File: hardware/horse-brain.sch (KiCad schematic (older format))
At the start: 12 parts

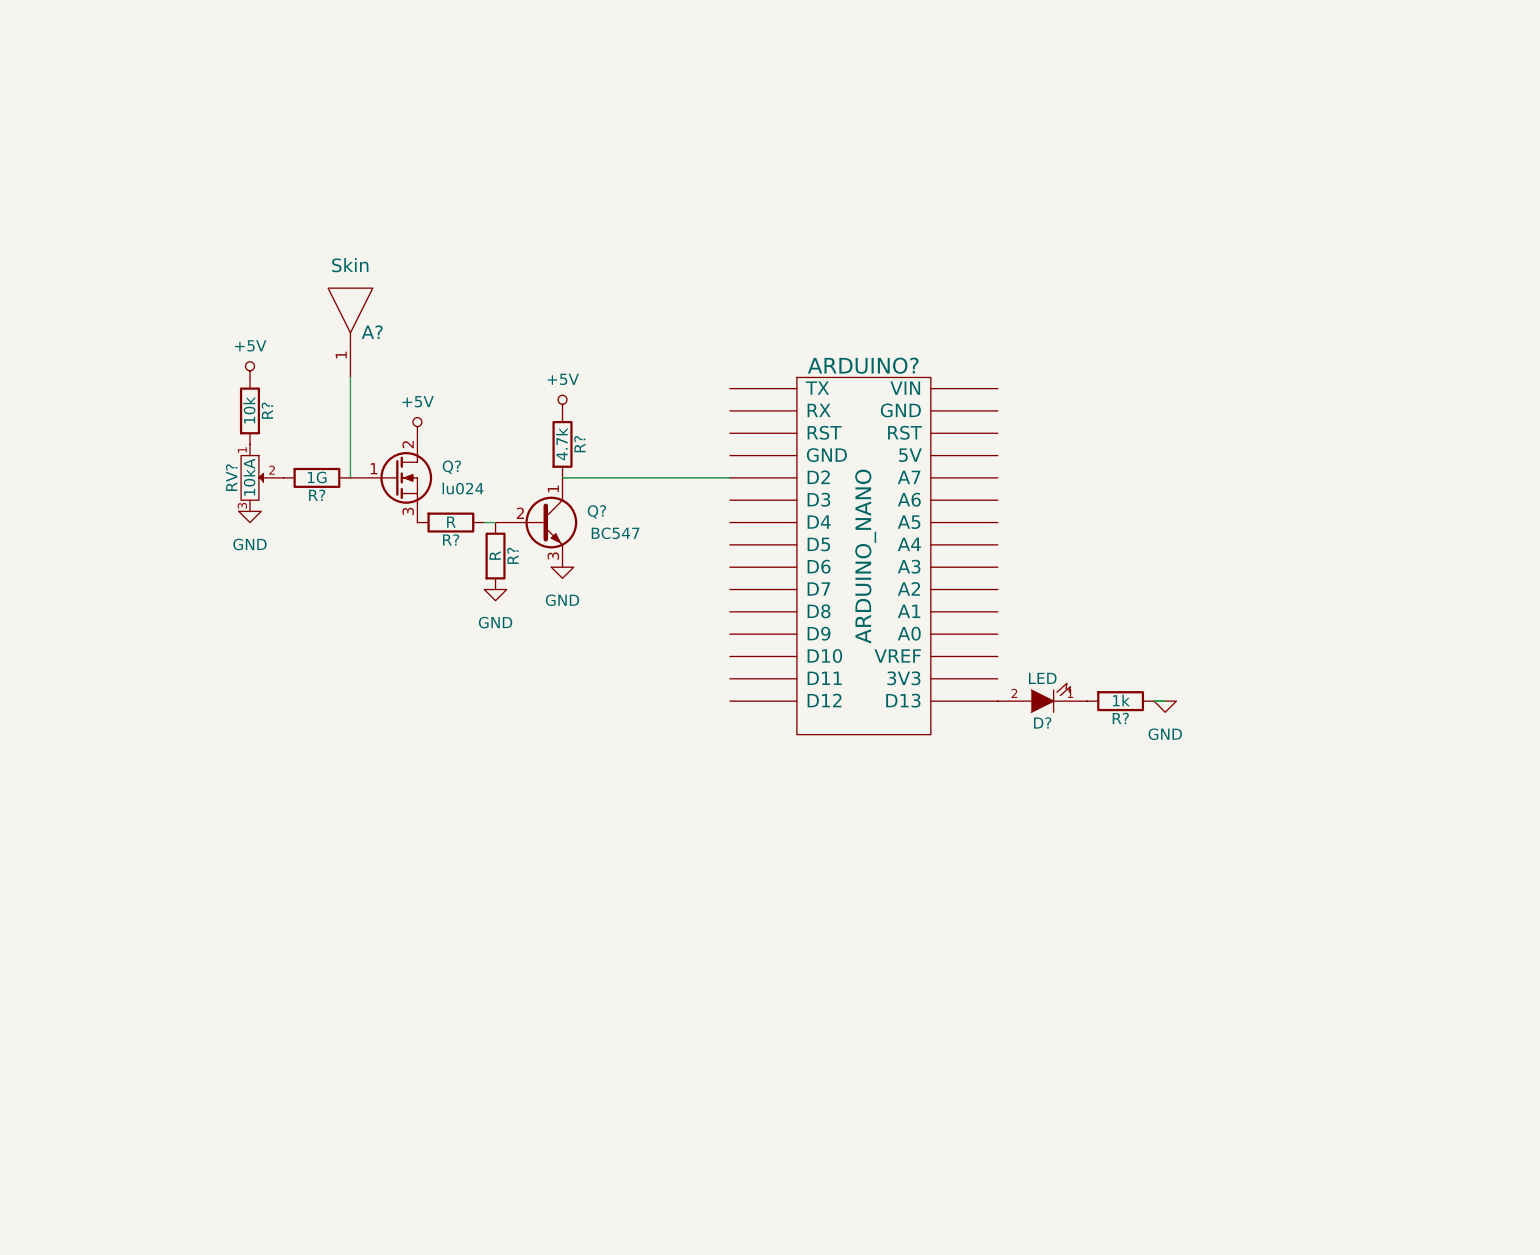
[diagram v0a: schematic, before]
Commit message: Add inverter interface to schematic
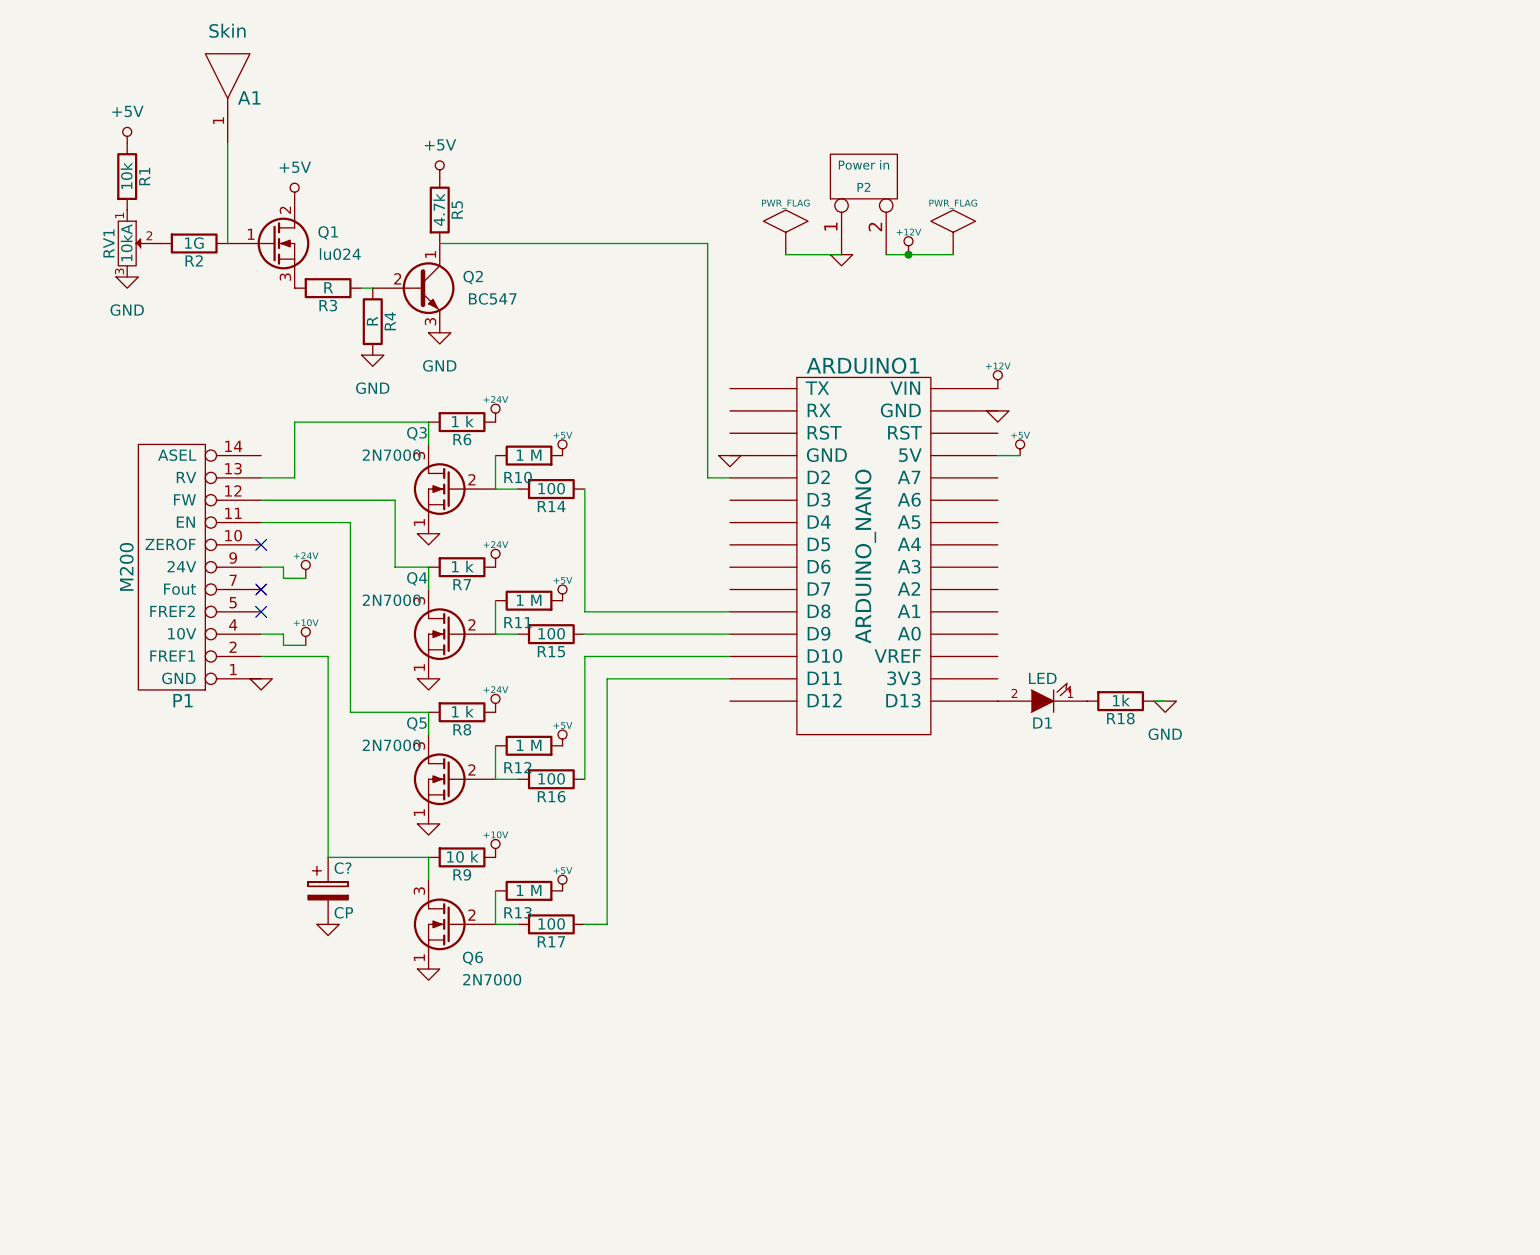
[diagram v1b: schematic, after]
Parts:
- added C?: CP, symbol CP
- added P1: M200, symbol M200
- added P2: Power in, symbol CONN_2
- added Q3, Q4, Q5, Q6: 2N7000, symbol Q_NMOS_SGD
- added R10, R11, R12, R13: 1 M, symbol R
- added R14, R15, R16, R17: 100, symbol R
- added R6, R7, R8: 1 k, symbol R
- added R9: 10 k, symbol R
- gave numbers to parts that had none: 12
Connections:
- net +5V: now also ARDUINO1.27 (5V), R10.2, R11.2, R12.2, R13.2
- net GND: now also ARDUINO1.29 (GND), ARDUINO1.4 (GND), C?.2, P1.1 (GND), P2.1 (P1), Q3.1 (S), Q4.1 (S), Q5.1 (S), Q6.1 (S)
- net at ARDUINO1.11 (D8): now also R14.1
- net at ARDUINO1.12 (D9): now also R15.1
- net at ARDUINO1.13 (D10): now also R16.1
- net at ARDUINO1.14 (D11): now also R17.1
- net +12V: now reaches ARDUINO1.30 (VIN)
- net +12V: now also P2.2 (PM)
- new net: P1.11 (EN), Q5.3 (D), R8.2
- new net: P1.12 (FW), Q4.3 (D), R7.2
- new net: P1.13 (RV), Q3.3 (D), R6.2
- new net: C?.1, P1.2 (FREF1), Q6.3 (D), R9.2
- new net: Q3.2 (G), R10.1, R14.2
- new net: Q4.2 (G), R11.1, R15.2
- new net: Q5.2 (G), R12.1, R16.2
- new net: Q6.2 (G), R13.1, R17.2
- new net +10V: P1.4 (10V), R9.1
- new net +24V: P1.9 (24V), R6.1, R7.1, R8.1
- no-connect marks 0 -> 3
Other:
- moved on the sheet: A1, Q1, Q2, R1, R2, R3, R4, R5, RV1

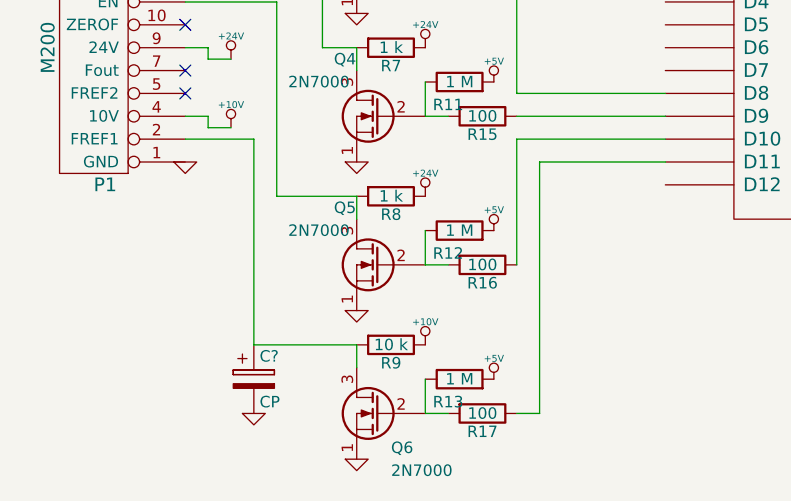
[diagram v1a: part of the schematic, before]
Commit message: First version of motor control code
Ensures that the interface to inverter works, but does not do anything
sensible yet. Also, there is a simplification regarding analog input to
inverter.
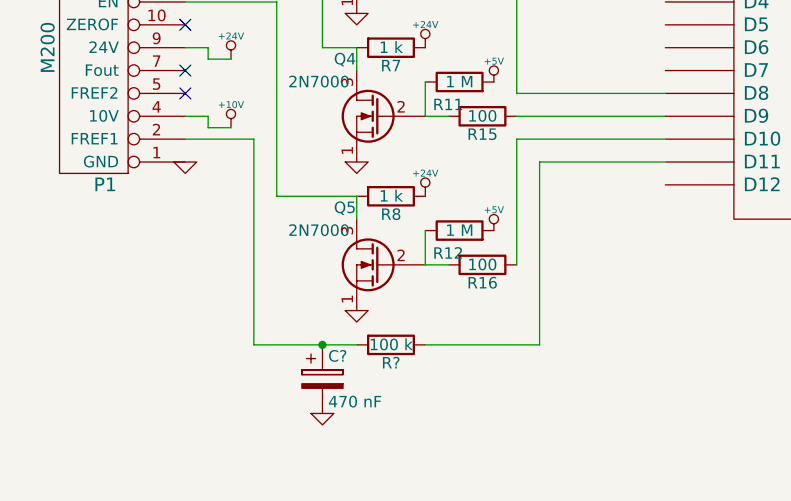
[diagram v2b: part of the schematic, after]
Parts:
- removed C?: CP, symbol CP
- removed Q6: 2N7000, symbol Q_NMOS_SGD
- removed R13: 1 M, symbol R
- removed R17: 100, symbol R
- removed R9: 10 k, symbol R
- added C?: 470 nF, symbol CP
- added R?: 100 k, symbol R
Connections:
- net GND: now also C?.2
- net at ARDUINO1.14 (D11): now also R?.1
- net at P1.2 (FREF1): now also C?.1, R?.2
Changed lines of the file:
@@
-	1    0    0    -1
-$EndComp
-$Comp
-L Q_NMOS_SGD Q6
-U 1 1 583F98D2
-P 4850 5500
-F 0 "Q6" H 4800 5350 50  0000 R CNN
-F 1 "2N7000" H 4800 5250 50  0000 R CNN
-F 2 "" H 5050 5600 50  0000 C CNN
-F 3 "" H 4850 5500 50  0000 C CNN
-	1    4850 5500
-	-1   0    0    -1
-$EndComp
-$Comp
-L R R13
-U 1 1 583F98D8
-P 5200 5350
-F 0 "R13" V 5100 5400 50  0000 C CNN
-F 1 "1 M" V 5200 5350 50  0000 C CNN
-F 2 "" V 5130 5350 50  0000 C CNN
-F 3 "" H 5200 5350 50  0000 C CNN
-	1    5200 5350
-	0    -1   -1   0
-$EndComp
-$Comp
-L R R17
-U 1 1 583F98DE
-P 5300 5500
-F 0 "R17" V 5380 5500 50  0000 C CNN
-F 1 "100" V 5300 5500 50  0000 C CNN
-F 2 "" V 5230 5500 50  0000 C CNN
-F 3 "" H 5300 5500 50  0000 C CNN
-	1    5300 5500
-	0    1    1    0
-$EndComp
-Wire Wire Line
-	5050 5500 5150 5500
-$Comp
-L +5V #PWR024
-U 1 1 583F98E5
-P 5350 5350
-F 0 "#PWR024" H 5350 5440 20  0001 C CNN
-F 1 "+5V" H 5350 5440 30  0000 C CNN
-F 2 "" H 5350 5350 60  0001 C CNN
-F 3 "" H 5350 5350 60  0001 C CNN
-	1    5350 5350
-	1    0    0    -1
-$EndComp
-Wire Wire Line
-	5050 5500 5050 5350
-$Comp
-L R R9
-U 1 1 583F98EC
-P 4900 5200
-F 0 "R9" V 4980 5200 50  0000 C CNN
-F 1 "10 k" V 4900 5200 50  0000 C CNN
-F 2 "" V 4830 5200 50  0000 C CNN
-F 3 "" H 4900 5200 50  0000 C CNN
-	1    4900 5200
-	0    1    1    0
-$EndComp
-Wire Wire Line
-	4750 5200 4750 5300
-$Comp
-L GND #PWR025
-U 1 1 583F98F9
-P 4750 5700
-F 0 "#PWR025" H 4750 5700 30  0001 C CNN
-F 1 "GND" H 4750 5630 30  0001 C CNN
-F 2 "" H 4750 5700 60  0001 C CNN
-F 3 "" H 4750 5700 60  0001 C CNN
-	1    4750 5700
 	1    0    0    -1
 $EndComp
@@
 	4100 4200 4000 4200
 NoConn ~ 4000 3800
-$Comp
-L +10V #PWR027
-U 1 1 583FD090
-P 5050 5200
-F 0 "#PWR027" H 5050 5150 20  0001 C CNN
-F 1 "+10V" H 5050 5300 30  0000 C CNN
-F 2 "" H 5050 5200 60  0001 C CNN
-F 3 "" H 5050 5200 60  0001 C CNN
-	1    5050 5200
-	1    0    0    -1
-$EndComp
-Wire Wire Line
-	4750 5200 4300 5200
 Wire Wire Line
 	4300 5200 4300 4300
 Wire Wire Line
 	4300 4300 4000 4300
-Wire Wire Line
-	5450 5500 5550 5500
-Wire Wire Line
-	5550 5500 5550 4400
 Wire Wire Line
 	5550 4400 6100 4400
@@
 Wire Wire Line
 	6600 2500 6350 2500
+Wire Wire Line
+	5550 5200 5550 4400
+$Comp
+L R R?
+U 1 1 5841B9D2
+P 4900 5200
+F 0 "R?" V 4980 5200 50  0000 C CNN
+F 1 "100 k" V 4900 5200 50  0000 C CNN
+F 2 "" V 4830 5200 50  0000 C CNN
+F 3 "" H 4900 5200 50  0000 C CNN
+	1    4900 5200
+	0    1    1    0
+$EndComp
 $Comp
 L CP C?
-U 1 1 5840E197
-P 4300 5350
-F 0 "C?" H 4325 5450 50  0000 L CNN
-F 1 "CP" H 4325 5250 50  0000 L CNN
-F 2 "" H 4338 5200 50  0000 C CNN
-F 3 "" H 4300 5350 50  0000 C CNN
-	1    4300 5350
+U 1 1 5841BAB8
+P 4600 5350
+F 0 "C?" H 4625 5450 50  0000 L CNN
+F 1 "470 nF" H 4625 5250 50  0000 L CNN
+F 2 "" H 4638 5200 50  0000 C CNN
+F 3 "" H 4600 5350 50  0000 C CNN
+	1    4600 5350
 	1    0    0    -1
 $EndComp
 $Comp
 L GND #PWR?
-U 1 1 5840E1EE
-P 4300 5500
-F 0 "#PWR?" H 4300 5500 30  0001 C CNN
-F 1 "GND" H 4300 5430 30  0001 C CNN
-F 2 "" H 4300 5500 60  0001 C CNN
-F 3 "" H 4300 5500 60  0001 C CNN
-	1    4300 5500
+U 1 1 5841BB07
+P 4600 5500
+F 0 "#PWR?" H 4600 5500 30  0001 C CNN
+F 1 "GND" H 4600 5430 30  0001 C CNN
+F 2 "" H 4600 5500 60  0001 C CNN
+F 3 "" H 4600 5500 60  0001 C CNN
+	1    4600 5500
 	1    0    0    -1
 $EndComp
+Wire Wire Line
+	5550 5200 5050 5200
+Wire Wire Line
+	4300 5200 4750 5200
+Connection ~ 4600 5200
 $EndSCHEMATC

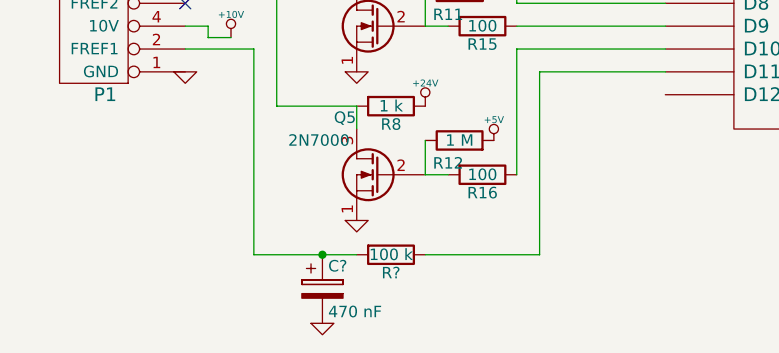
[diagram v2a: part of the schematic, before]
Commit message: Code and hardware fix for motor frequency input
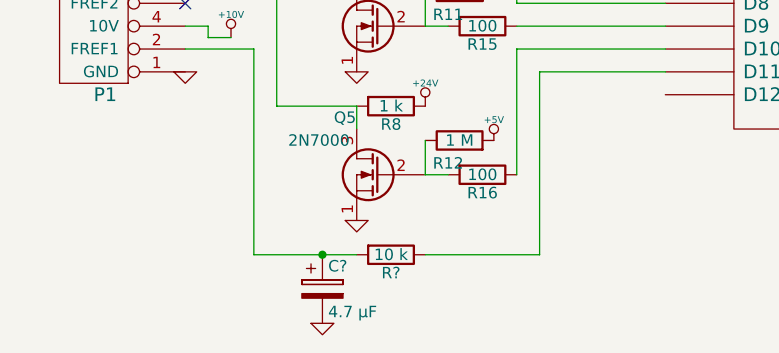
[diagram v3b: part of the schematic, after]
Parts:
- C?: value 470 nF -> 4.7 μF
- R?: value 100 k -> 10 k
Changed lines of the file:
@@
 P 4900 5200
 F 0 "R?" V 4980 5200 50  0000 C CNN
-F 1 "100 k" V 4900 5200 50  0000 C CNN
+F 1 "10 k" V 4900 5200 50  0000 C CNN
 F 2 "" V 4830 5200 50  0000 C CNN
 F 3 "" H 4900 5200 50  0000 C CNN
@@
 P 4600 5350
 F 0 "C?" H 4625 5450 50  0000 L CNN
-F 1 "470 nF" H 4625 5250 50  0000 L CNN
+F 1 "4.7 μF" H 4625 5250 50  0000 L CNN
 F 2 "" H 4638 5200 50  0000 C CNN
 F 3 "" H 4600 5350 50  0000 C CNN
